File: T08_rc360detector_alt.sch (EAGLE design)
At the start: 55 parts, among them IC1 LM317MSTT3, IC2 LM317MSTT3, IC3 LM1117, U2 ATMEGA328P_PDIP, X1 SSW-101-02-S-D, X3 SSW-101-02-S-D, X4 87758-0616, X5 87758-0616, X6 SSW-104-02-S-Q

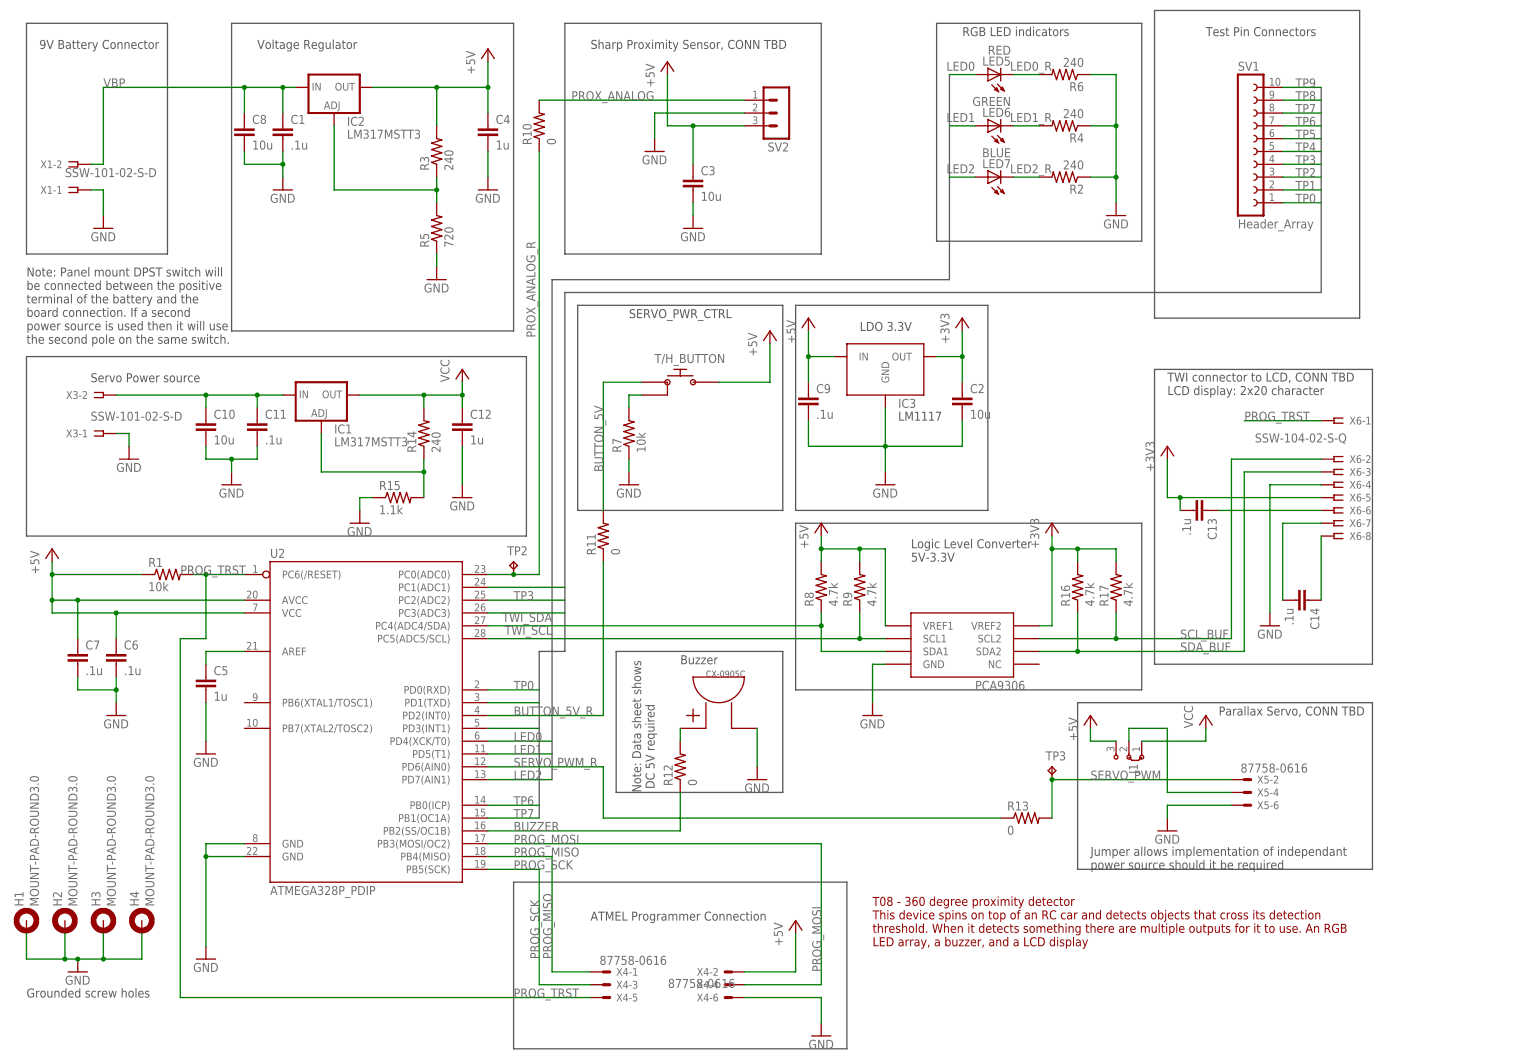
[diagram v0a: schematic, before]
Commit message: Finished preliminary layout
Finished layout after feedback today
Also made an alternate layout that I feel is cleaner and experimented
with importing silkscreen images.
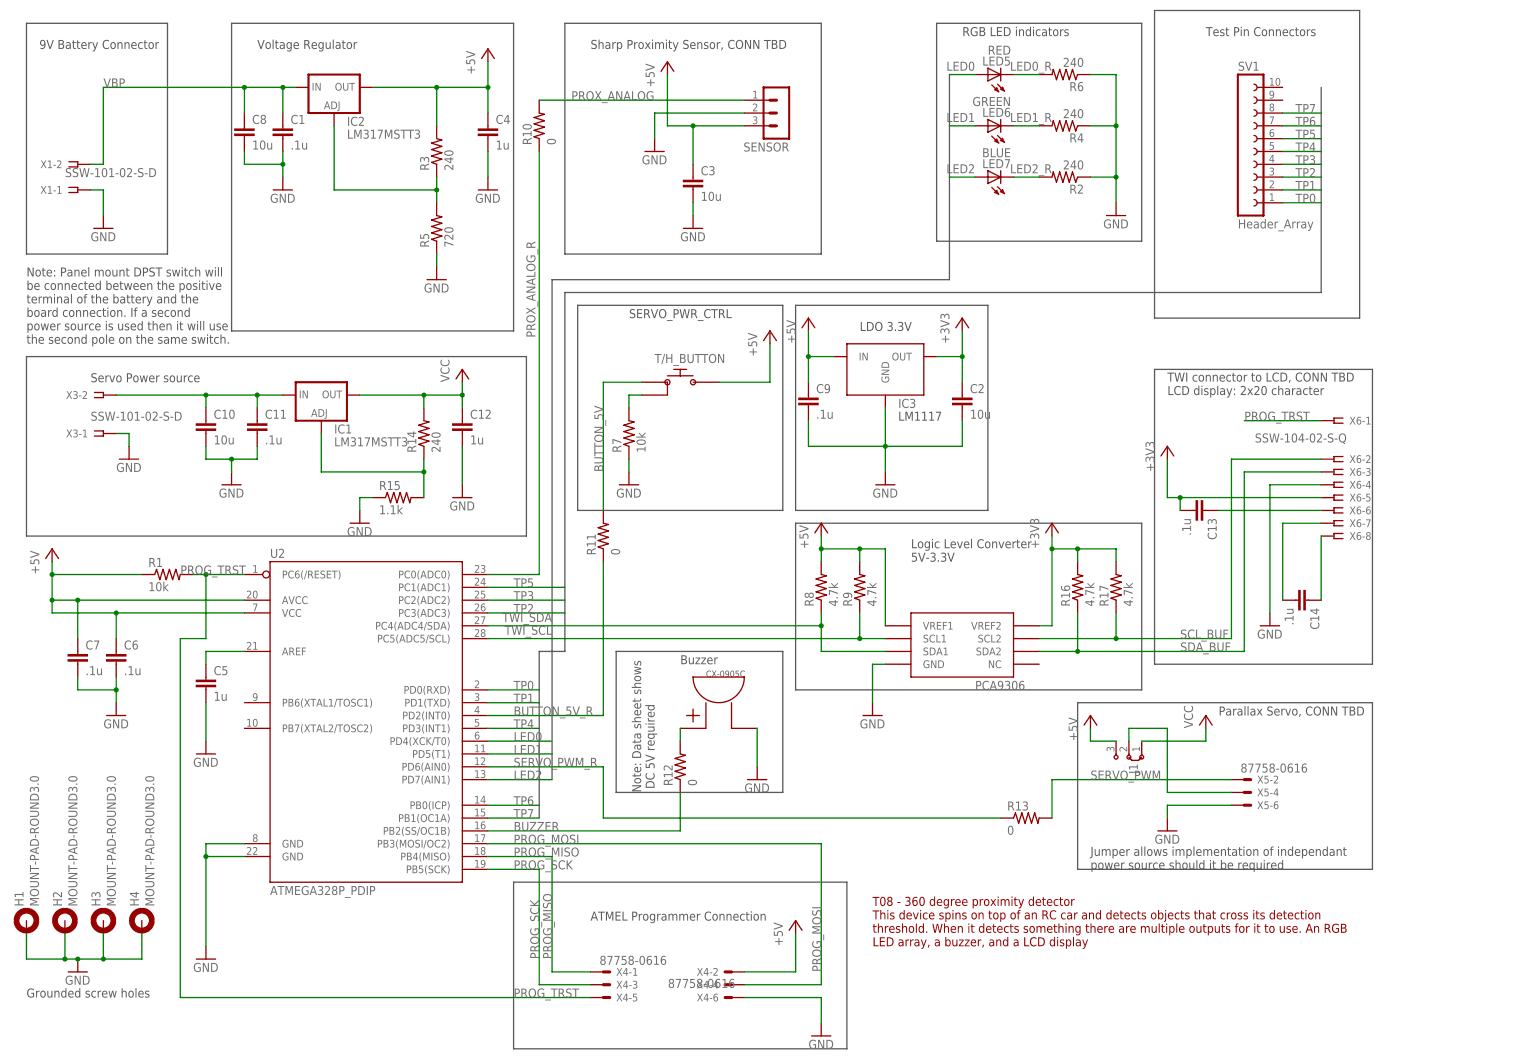
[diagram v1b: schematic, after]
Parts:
- removed TP2, TP3: TPPAD1-17, testpad:TPPAD1-17
- renumbered SV2 to SENSOR
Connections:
- removed net TP8: SV1.9
- removed net TP9: SV1.10
- net PROX_ANALOG_R: no longer TP2.TP
- net SERVO_PWM: no longer TP3.TP
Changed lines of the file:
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@@
 <part name="P+3" library="supply1" deviceset="+5V" device=""/>
 <part name="P+5" library="supply1" deviceset="+5V" device=""/>
-<part name="TP2" library="testpad" deviceset="TP" device="PAD1-17"/>
-<part name="TP3" library="testpad" deviceset="TP" device="PAD1-17"/>
 <part name="R2" library="rcl" deviceset="R-US_" device="R0805" value="240"/>
 <part name="R4" library="rcl" deviceset="R-US_" device="R0805" value="240"/>
@@
 <part name="R15" library="rcl" deviceset="R-US_" device="R0805" value="1.1k"/>
 <part name="P+4" library="supply1" deviceset="VCC" device=""/>
-<part name="SV2" library="con-lstb" deviceset="MA03-1" device=""/>
+<part name="SENSOR" library="con-lstb" deviceset="MA03-1" device=""/>
 <part name="CX-0905C" library="360prox" deviceset="CX-0905C" device=""/>
 <part name="J1" library="jumper" deviceset="J2" device="X2MM"/>
@@
 <instance part="P+3" gate="1" x="134.62" y="198.12"/>
 <instance part="P+5" gate="1" x="160.02" y="27.94"/>
-<instance part="TP2" gate="G$1" x="104.14" y="99.06"/>
-<instance part="TP3" gate="G$1" x="210.82" y="58.42"/>
 <instance part="R2" gate="G$1" x="213.36" y="175.26" rot="R180"/>
 <instance part="R4" gate="G$1" x="213.36" y="185.42" rot="R180"/>
@@
 <instance part="R15" gate="G$1" x="81.28" y="111.76"/>
 <instance part="P+4" gate="VCC" x="93.98" y="137.16"/>
-<instance part="SV2" gate="G$1" x="157.48" y="187.96" rot="R180"/>
+<instance part="SENSOR" gate="G$1" x="157.48" y="187.96" rot="R180"/>
 <instance part="CX-0905C" gate="G$1" x="144.78" y="68.58"/>
 <instance part="J1" gate="G$1" x="226.06" y="60.96" rot="R270"/>
@@
 <wire x1="139.7" y1="185.42" x2="139.7" y2="177.8" width="0.1524" layer="91"/>
 <pinref part="C3" gate="G$1" pin="1"/>
-<pinref part="SV2" gate="G$1" pin="3"/>
+<pinref part="SENSOR" gate="G$1" pin="3"/>
 <wire x1="139.7" y1="185.42" x2="149.86" y2="185.42" width="0.1524" layer="91"/>
 <junction x="139.7" y="185.42"/>
@@
 <pinref part="GND6" gate="1" pin="GND"/>
 <wire x1="132.08" y1="187.96" x2="132.08" y2="182.88" width="0.1524" layer="91"/>
-<pinref part="SV2" gate="G$1" pin="2"/>
+<pinref part="SENSOR" gate="G$1" pin="2"/>
 <wire x1="132.08" y1="187.96" x2="149.86" y2="187.96" width="0.1524" layer="91"/>
 </segment>
@@
 <segment>
 <label x="218.44" y="55.88" size="1.778" layer="95"/>
-<pinref part="TP3" gate="G$1" pin="TP"/>
 <wire x1="210.82" y1="55.88" x2="246.38" y2="55.88" width="0.1524" layer="91"/>
 <pinref part="X5" gate="-2" pin="S"/>
 <pinref part="R13" gate="G$1" pin="2"/>
 <wire x1="210.82" y1="48.26" x2="210.82" y2="55.88" width="0.1524" layer="91"/>
-<junction x="210.82" y="55.88"/>
 </segment>
 </net>
@@
 <wire x1="109.22" y1="190.5" x2="149.86" y2="190.5" width="0.1524" layer="91"/>
 <pinref part="R10" gate="G$1" pin="2"/>
-<pinref part="SV2" gate="G$1" pin="1"/>
+<pinref part="SENSOR" gate="G$1" pin="1"/>
 </segment>
 </net>
@@
 <pinref part="U2" gate="G$1" pin="PC3(ADC3)"/>
 <wire x1="99.06" y1="88.9" x2="114.3" y2="88.9" width="0.1524" layer="91"/>
+<label x="104.14" y="88.9" size="1.778" layer="95"/>
 </segment>
 </net>
@@
 <pinref part="U2" gate="G$1" pin="PC1(ADC1)"/>
 <wire x1="99.06" y1="93.98" x2="114.3" y2="93.98" width="0.1524" layer="91"/>
+<label x="104.14" y="93.98" size="1.778" layer="95"/>
 </segment>
 </net>
@@
 </segment>
 </net>
-<net name="TP8" class="0">
-<segment>
-<pinref part="SV1" gate="G$1" pin="9"/>
-<wire x1="256.54" y1="190.5" x2="264.16" y2="190.5" width="0.1524" layer="91"/>
-<label x="259.08" y="190.5" size="1.778" layer="95"/>
-</segment>
-</net>
-<net name="TP9" class="0">
-<segment>
-<pinref part="SV1" gate="G$1" pin="10"/>
-<wire x1="256.54" y1="193.04" x2="264.16" y2="193.04" width="0.1524" layer="91"/>
-<label x="259.08" y="193.04" size="1.778" layer="95"/>
-</segment>
-</net>
 <net name="TP4" class="0">
 <segment>
@@
 <pinref part="U2" gate="G$1" pin="PD3(INT1)"/>
 <wire x1="99.06" y1="66.04" x2="109.22" y2="66.04" width="0.1524" layer="91"/>
+<label x="104.14" y="66.04" size="1.778" layer="95"/>
 </segment>
 </net>
 <net name="PROX_ANALOG_R" class="0">
 <segment>
-<pinref part="TP2" gate="G$1" pin="TP"/>
-<junction x="104.14" y="96.52"/>
-<wire x1="99.06" y1="96.52" x2="104.14" y2="96.52" width="0.1524" layer="91"/>
-<wire x1="104.14" y1="96.52" x2="109.22" y2="96.52" width="0.1524" layer="91"/>
+<wire x1="99.06" y1="96.52" x2="109.22" y2="96.52" width="0.1524" layer="91"/>
 <pinref part="R10" gate="G$1" pin="1"/>
 <wire x1="109.22" y1="96.52" x2="109.22" y2="180.34" width="0.1524" layer="91"/>
@@
 <pinref part="U2" gate="G$1" pin="PD1(TXD)"/>
 <wire x1="99.06" y1="71.12" x2="109.22" y2="71.12" width="0.1524" layer="91"/>
-</segment>
-</net>
+<label x="104.14" y="71.12" size="1.778" layer="95"/>
+</segment>
+</net>
